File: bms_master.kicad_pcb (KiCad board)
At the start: 4 copper layers, 85 x 65 mm, 98 parts, among them J1 Conn_01x02, J2 Conn_01x02, J3 Conn_01x02, J4 Conn_01x04, J5 Conn_01x04, J6 Conn_01x06, J7 Conn_01x05, J8 Conn_01x05, Q1 FDV303N, Q2 FDV304P, Q3 FDV304P, SW1 SW_Push, U1 TPS7B88, U2 MCP1700x-330xxMB, U3 STM32F103C8Tx, U4 SN65HVD1050D, U5 M24C64-R, U6 MAX6126, U7 MAX11163, U8 741G3157, U9 TPS25961, Y1 8M

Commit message: *: Use more suitable MOSFETs in the shutdown circuit
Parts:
- Q1: value FDV303N -> PMV15ENE
- Q2, Q3: value FDV304P -> PMV74EPE

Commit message: *: Change shutdown MOSFET gate resistors to 1k
This provides more protection and reduces BOM count.
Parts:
- R22, R24, R4: value 100 -> 1k
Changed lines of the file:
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@@
 			)
 		)
-		(property "Value" "100"
+		(property "Value" "1k"
 			(at 0 1.43 0)
 			(layer "F.Fab")
@@
 			)
 		)
-		(property "Dist #" "C22775"
+		(property "Dist #" "C21190"
 			(at 0 0 0)
 			(unlocked yes)
@@
 			)
 		)
-		(property "Mfr #" "0603WAF1000T5E"
+		(property "Mfr #" "0603WAF1001T5E"
 			(at 0 0 0)
 			(unlocked yes)
@@
 			)
 		)
-		(property "Value" "100"
+		(property "Value" "1k"
 			(at 0 1.43 0)
 			(layer "F.Fab")
@@
 			)
 		)
-		(property "Dist #" "C22775"
+		(property "Dist #" "C21190"
 			(at 0 0 0)
 			(unlocked yes)
@@
 			)
 		)
-		(property "Mfr #" "0603WAF1000T5E"
+		(property "Mfr #" "0603WAF1001T5E"
 			(at 0 0 0)
 			(unlocked yes)
@@
 			)
 		)
-		(property "Value" "100"
+		(property "Value" "1k"
 			(at 0 1.43 0)
 			(layer "F.Fab")
@@
 			)
 		)
-		(property "Dist #" "C22775"
+		(property "Dist #" "C21190"
 			(at 0 0 0)
 			(unlocked yes)
@@
 			)
 		)
-		(property "Mfr #" "0603WAF1000T5E"
+		(property "Mfr #" "0603WAF1001T5E"
 			(at 0 0 0)
 			(unlocked yes)

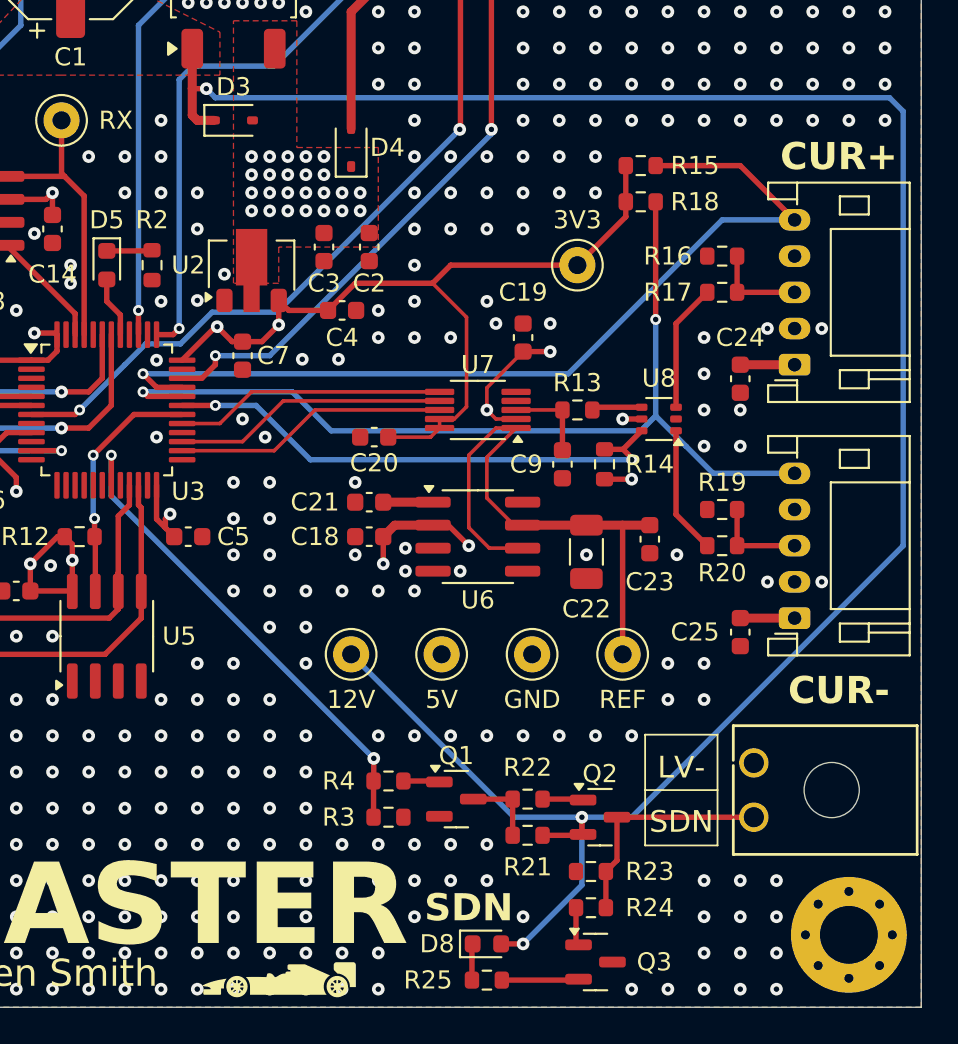
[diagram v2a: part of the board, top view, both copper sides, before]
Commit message: *: Add a current limiting resistor to the shutdown output
This reduces the output level to around 10.9 volts.
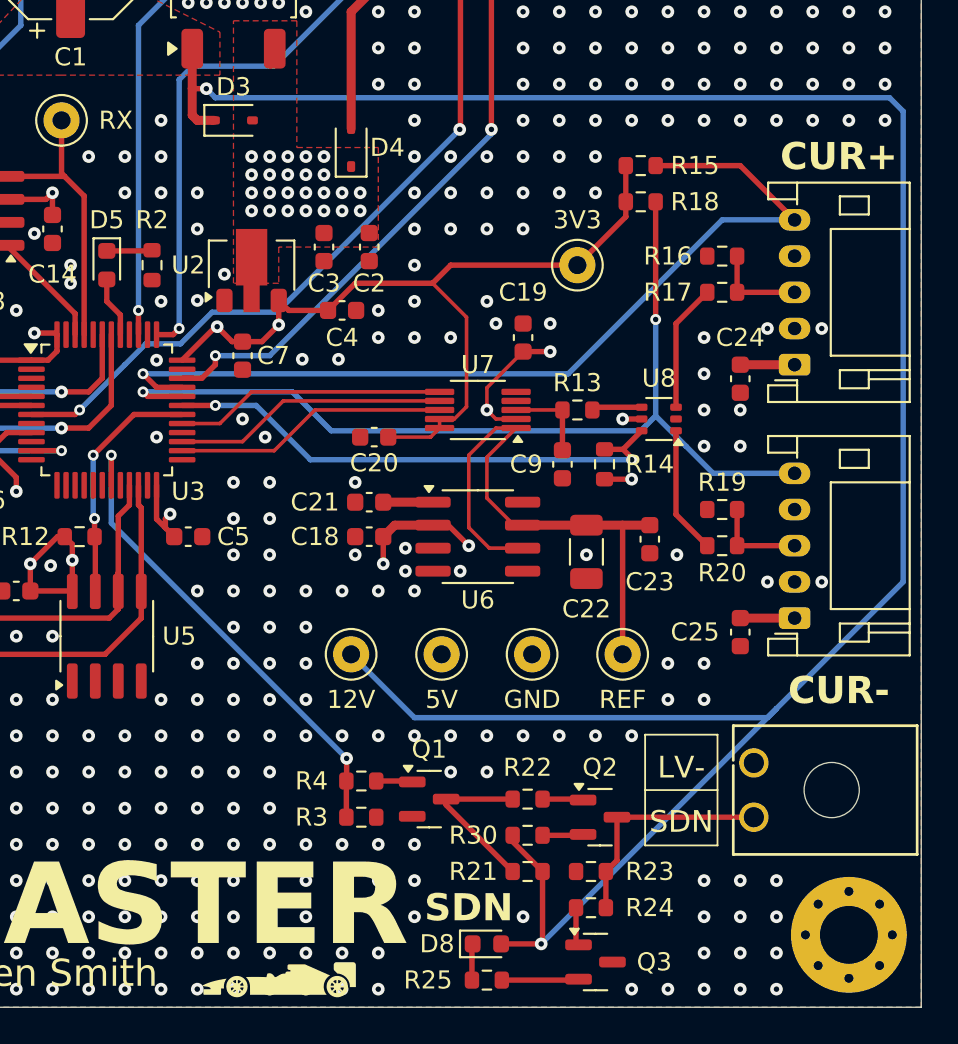
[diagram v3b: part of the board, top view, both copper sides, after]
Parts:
- added R30: 1k, Resistor_SMD:R_0603_1608Metric, F.Cu at (128.2, 85.5)
- moved R21 2.00 mm to (128.2, 87.5)
- moved Q1 1.50 mm to (122.8, 83.5)
- moved R3 1.50 mm to (119.1, 84.5)
- moved R4 1.50 mm to (119.1, 82.5)
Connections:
- Q2 pad 2: +12V -> Net-(Q2-S)
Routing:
- net +12V: track 168.5 -> 179.6 mm, vias 6 -> 5
- net Net-(Q1-D): track 4.19 -> 9.21 mm
- net Net-(Q2-S): track 0.00 -> 2.35 mm
- net SDN_MCU: track 27.7 -> 27.0 mm
- net GND: vias 499 -> 500

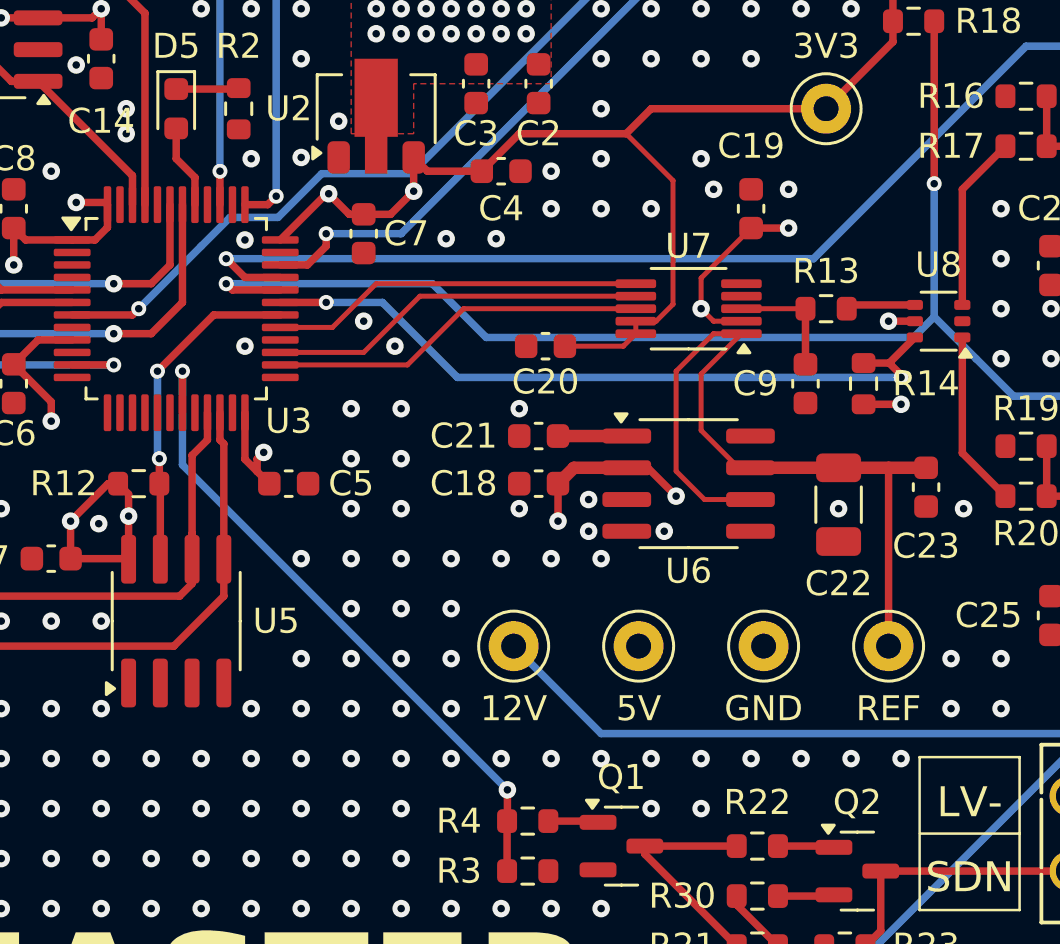
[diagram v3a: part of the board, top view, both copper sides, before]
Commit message: *: Connect the reference to an STM ADC pin
Also change the EEPROM_WC pin.
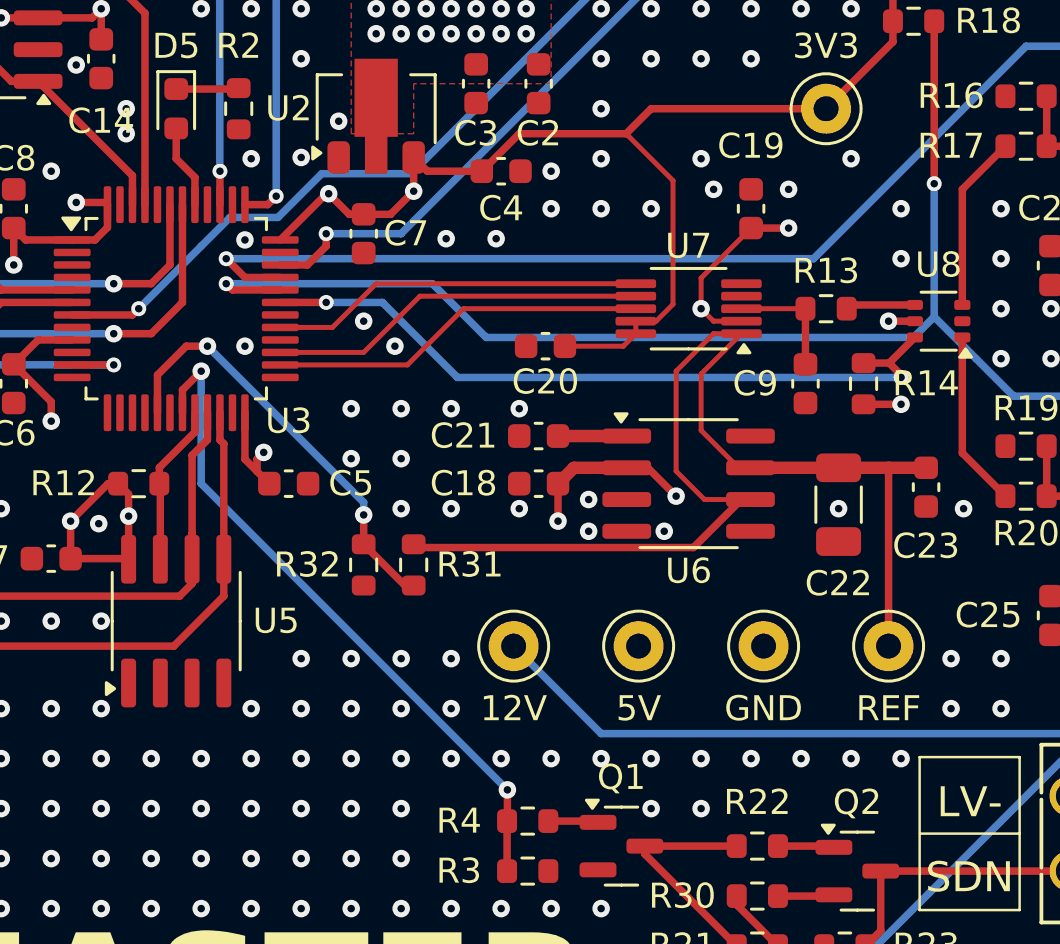
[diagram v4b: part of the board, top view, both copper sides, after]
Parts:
- added R31: 10k, Resistor_SMD:R_0603_1608Metric, F.Cu at (114.5, 72.2)
- added R32: 10k, Resistor_SMD:R_0603_1608Metric, F.Cu at (112.5, 72.2)
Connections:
- U3 pad 17: unconnected-(U3-PA7-Pad17) -> REF_SAMPL
- U3 pad 20: unconnected-(U3-PB2-Pad20) -> EEPROM_WC
- U3 pad 30: EEPROM_WC -> unconnected-(U3-PA9-Pad30)
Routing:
- net REF_SAMPL: track 0.00 -> 17.2 mm, vias 0 -> 2
- net /REF: track 31.5 -> 45.8 mm
- net EEPROM_WC: track 13.4 -> 6.41 mm, vias 2 -> 0
- net GND: vias 500 -> 494

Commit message: *: Update 12 volt rail measurement circuit
Select a zener and increase the upper resistor slightly.
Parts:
- R5: value 36k -> 43k
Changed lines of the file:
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@@
 			)
 		)
-		(property "Value" "36k"
+		(property "Value" "43k"
 			(at 0 1.43 90)
 			(layer "F.Fab")
@@
 			)
 		)
+		(property "Dist" "LCSC"
+			(at 0 0 270)
+			(unlocked yes)
+			(layer "F.Fab")
+			(hide yes)
+			(effects
+				(font
+					(size 1 1)
+					(thickness 0.15)
+				)
+			)
+		)
+		(property "Dist #" "C3739733"
+			(at 0 0 270)
+			(unlocked yes)
+			(layer "F.Fab")
+			(hide yes)
+			(effects
+				(font
+					(size 1 1)
+					(thickness 0.15)
+				)
+			)
+		)
+		(property "Mfr" "VISHAY"
+			(at 0 0 270)
+			(unlocked yes)
+			(layer "F.Fab")
+			(hide yes)
+			(effects
+				(font
+					(size 1 1)
+					(thickness 0.15)
+				)
+			)
+		)
+		(property "Mfr #" "BZX384C3V6"
+			(at 0 0 270)
+			(unlocked yes)
+			(layer "F.Fab")
+			(hide yes)
+			(effects
+				(font
+					(size 1 1)
+					(thickness 0.15)
+				)
+			)
+		)
 		(property ki_fp_filters "TO-???* *_Diode_* *SingleDiode* D_*")
 		(sheetname "/")
 		(sheetfile "bms_master.kicad_sch")
-		(attr smd dnp)
+		(attr smd)
 		(fp_line
 			(start -1.61 0.85)

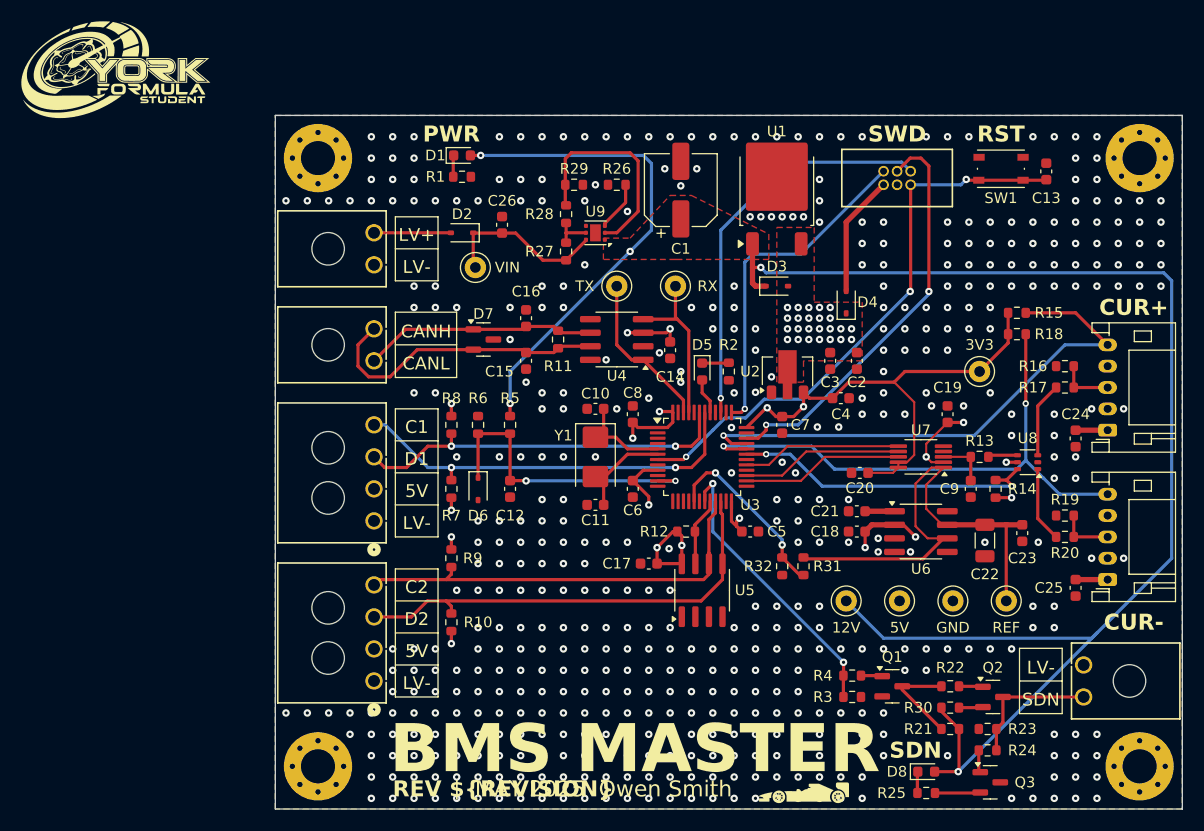
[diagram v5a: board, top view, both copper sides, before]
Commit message: *: Add TPS3851 watchdog IC
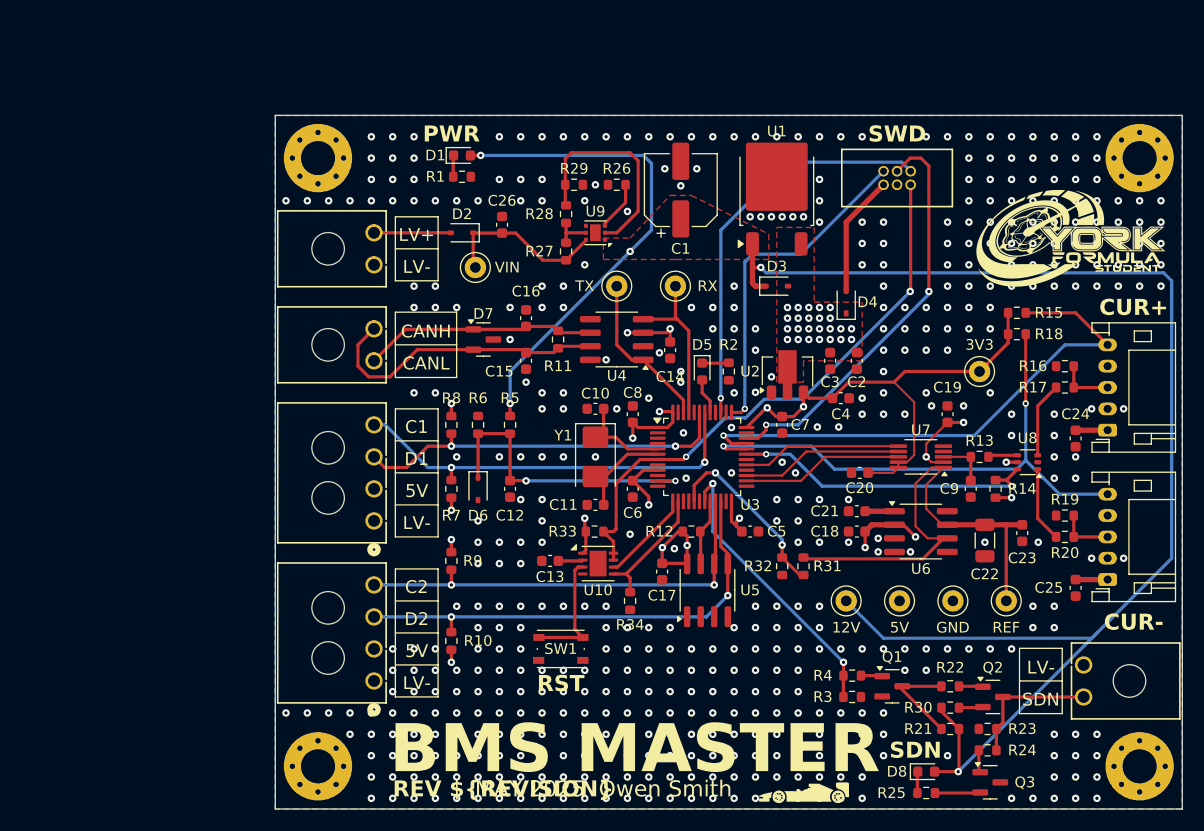
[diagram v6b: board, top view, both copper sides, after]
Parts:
- added R33: 10k, Resistor_SMD:R_0603_1608Metric, F.Cu at (94.9, 69.0)
- added R34: 10k, Resistor_SMD:R_0603_1608Metric, F.Cu at (98.2, 75.5)
- added U10: TPS3851, Package_SON:VSON-8-1EP_3x3mm_P0.65mm_EP1.6x2.4mm, F.Cu at (95.2, 72.0)
- moved G*** 90.9 mm to (139.5, 41.5)
- moved SW1 61.0 mm to (91.8, 80.0)
- moved C13 59.1 mm to (90.8, 71.8), turned to 180 degrees
- moved R10 1.75 mm to (81.5, 79.2)
- moved C17 1.46 mm to (101.2, 72.8), turned to -90 degrees
- moved R12 0.50 mm to (104.0, 69.0)
- moved U5 0.50 mm to (105.5, 74.5)
- moved R9 0.25 mm to (81.5, 71.8)
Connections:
- C13 pad 1: /NRST -> Net-(U10-CWD)
- J6 pad 5: /NRST -> NRST
- SW1 pad 1: /NRST -> GND
- SW1 pad 2: GND -> Net-(U10-~{MR})
- U3 pad 13: unconnected-(U3-PA3-Pad13) -> WDI
- U3 pad 14: unconnected-(U3-PA4-Pad14) -> WDS
- U3 pad 7: /NRST -> NRST
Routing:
- net NRST: track 0.00 -> 53.6 mm, vias 0 -> 2
- net /NRST: track 53.2 -> 0.00 mm, vias 3 -> 0
- net WDS: track 0.00 -> 11.9 mm
- net Net-(U10-~{MR}): track 0.00 -> 11.6 mm
- net WDI: track 0.00 -> 8.70 mm
- net +3V3: track 63.0 -> 66.5 mm, vias 6 -> 7
- net Net-(U10-CWD): track 0.00 -> 2.32 mm
- net SDA2: track 42.9 -> 44.5 mm, vias 0 -> 2
- net SCL2: track 40.8 -> 41.2 mm, vias 0 -> 2
- net GND: vias 494 -> 495
